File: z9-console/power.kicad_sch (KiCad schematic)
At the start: 29 parts, among them U1 B0505XT-1WR3, U22 TLV76733DRVx, U6 LMR14006YDDCR

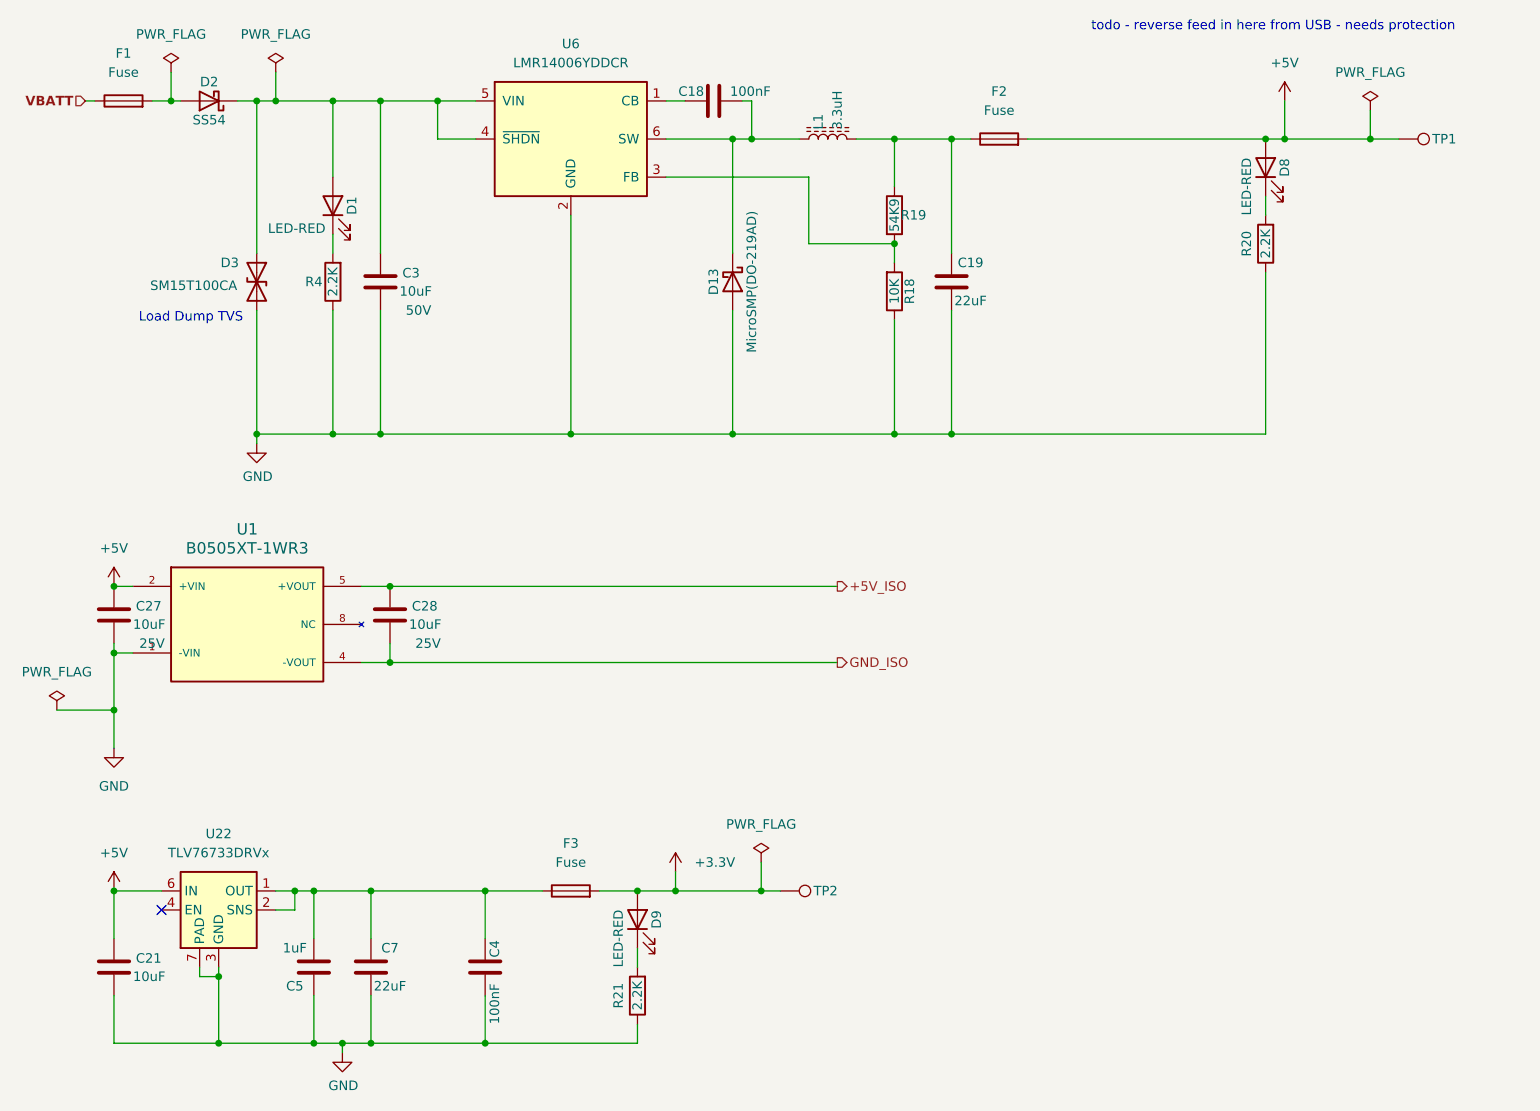
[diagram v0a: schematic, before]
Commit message: lcd power switch-- add new accelerometer
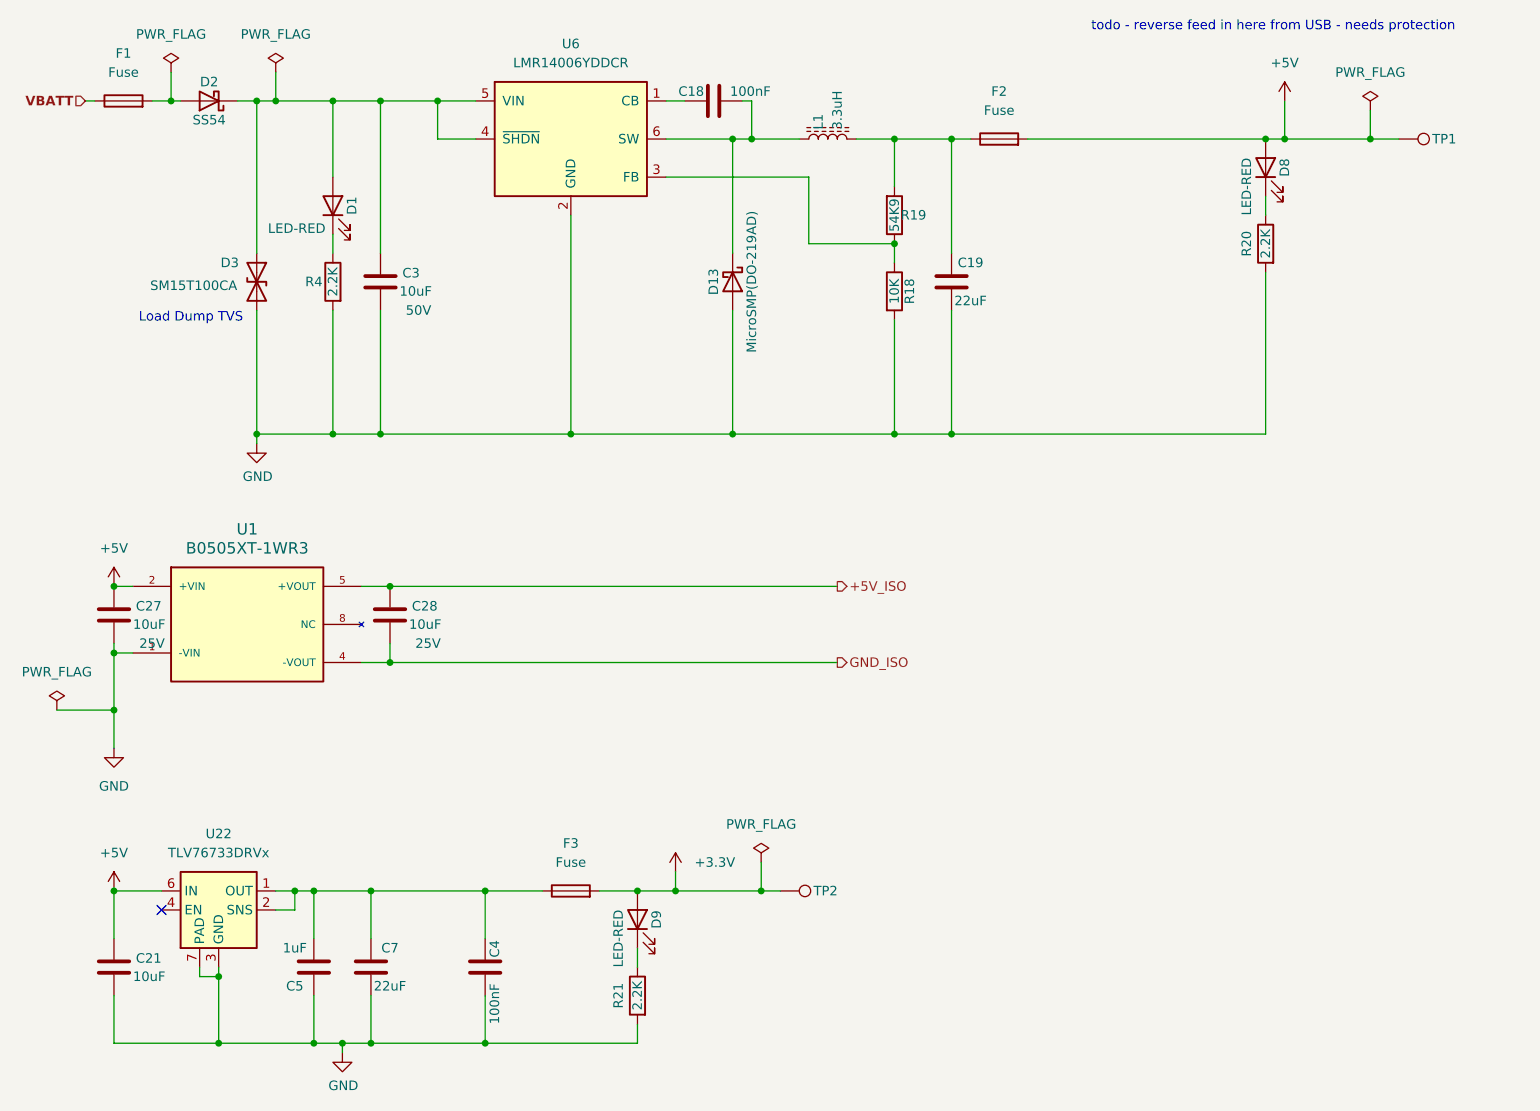
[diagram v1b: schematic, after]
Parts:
- R18: footprint Resistor_SMD:R_0603_1608Metric -> PCM_JLCPCB:R_0402; symbol Device:R -> dnt_global:Resistor_0402,10kΩ; Attrition Qty (none) -> 10; Category (none) -> Resistors,Chip Resistor - Surface Mount; Class (none) -> Basic Component; LCSC C25804 -> C25744; Manufacturer StackPole -> UNI-ROYAL(Uniroyal Elec); Minimum Qty (none) -> 20; Operating Temperature Range (none) -> -55°C~+155°C; Overload Voltage (Max) (none) -> 50V; Part (none) -> 0402WGF1002TCE; Part # RMCF0603JT10K0 -> (none); Power(Watts) (none) -> 62.5mW; Price (none) -> 0.004USD; Process (none) -> SMT; Resistance (none) -> 10kΩ; Stock (none) -> 24372091; Temperature Coefficient (none) -> ±100ppm/°C; Tolerance (none) -> ±1%; Type (none) -> Thick Film Resistors; VEND DIGI -> (none); VEND# RMCF0603JT10K0CT-ND -> (none)
- R19: footprint Resistor_SMD:R_0603_1608Metric -> PCM_JLCPCB:R_0402; symbol Device:R -> dnt_global:Resistor_0402,10kΩ; Attrition Qty (none) -> 10; Category (none) -> Resistors,Chip Resistor - Surface Mount; Class (none) -> Basic Component; LCSC C185321 -> C25744; Manufacturer YAGEO -> UNI-ROYAL(Uniroyal Elec); Minimum Qty (none) -> 20; Operating Temperature Range (none) -> -55°C~+155°C; Overload Voltage (Max) (none) -> 50V; Part (none) -> 0402WGF1002TCE; Part # RC0603FR-0754K9L -> (none); Power(Watts) (none) -> 62.5mW; Price (none) -> 0.004USD; Process (none) -> SMT; Resistance (none) -> 10kΩ; Silkscreen Hmm -> (none); Stock (none) -> 24372091; Temperature Coefficient (none) -> ±100ppm/°C; Tolerance (none) -> ±1%; Type (none) -> Thick Film Resistors
- R20, R21, R4: footprint Resistor_SMD:R_0603_1608Metric -> PCM_JLCPCB:R_0402; symbol Device:R -> dnt_global:Resistor_0402,10kΩ; Attrition Qty (none) -> 10; Category (none) -> Resistors,Chip Resistor - Surface Mount; Class (none) -> Basic Component; LCSC C4190 -> C25744; Manufacturer (none) -> UNI-ROYAL(Uniroyal Elec); Minimum Qty (none) -> 20; Operating Temperature Range (none) -> -55°C~+155°C; Overload Voltage (Max) (none) -> 50V; Part (none) -> 0402WGF1002TCE; Power(Watts) (none) -> 62.5mW; Price (none) -> 0.004USD; Process (none) -> SMT; Resistance (none) -> 10kΩ; Stock (none) -> 24372091; Temperature Coefficient (none) -> ±100ppm/°C; Tolerance (none) -> ±1%; Type (none) -> Thick Film Resistors

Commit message: change MEMS device
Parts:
- U5: renamed from U22; symbol Regulator_Linear:TLV76733DRVx -> dnt_global:TLV76733DRVx
- renumbered C19 to C10, C27 to C2, C21 to C3, C5 to C4, C7 to C5, C3 to C6, C28 to C7, C4 to C8, C18 to C9, D1 to D4, D9 to D5, D13 to D6, D8 to D7, F1 to F2, F2 to F4, L1 to L2, R18 to R10, R20 to R11, R4 to R7, R21 to R8, R19 to R9, TP1 to TP3, U1 to U6, U6 to U7
